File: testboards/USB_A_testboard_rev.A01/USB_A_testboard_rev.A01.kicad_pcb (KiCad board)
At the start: 2 copper layers, 18 x 12 mm, 10 parts, among them J1 USB_A_PCB_Edge_receptacle, J2 Conn_01x04, U1 USBLC6-2SC6

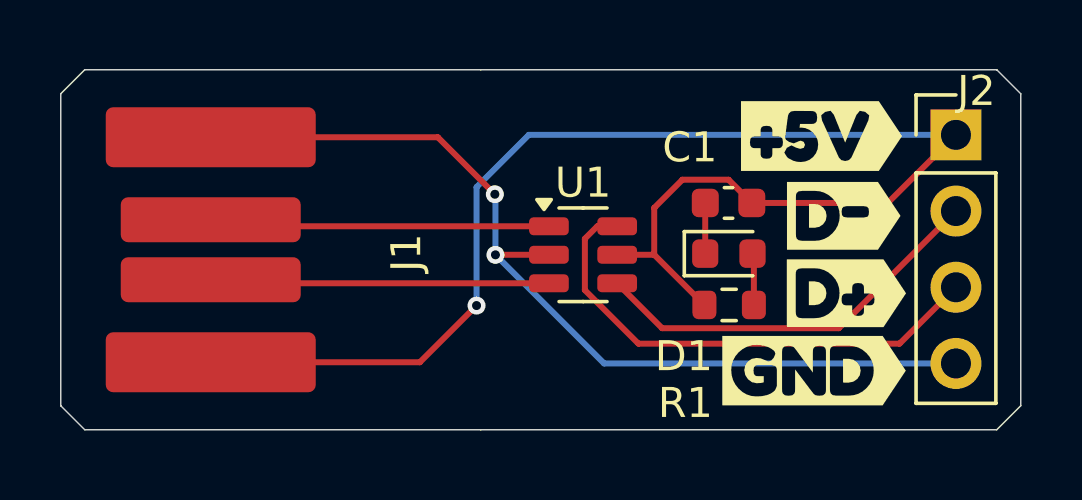
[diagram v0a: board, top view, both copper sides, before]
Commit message: Re-work test board to minimal USB-A PCB Plug
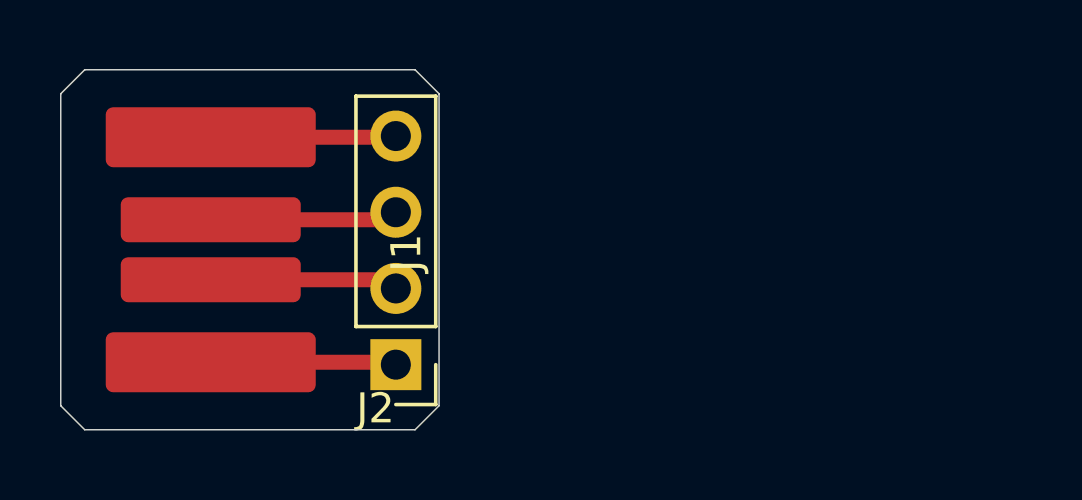
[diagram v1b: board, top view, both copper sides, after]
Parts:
- removed C1: 0.1u, Capacitor_SMD:C_0603_1608Metric
- removed D1: GREEN, LED_SMD:LED_0603_1608Metric
- removed R1: 1K, Resistor_SMD:R_0603_1608Metric
- removed U1: USBLC6-2SC6, Package_TO_SOT_SMD:SOT-23-6
- kibuzzard-65ECED05, kibuzzard-65ECED21, kibuzzard-65ECED2E, kibuzzard-65ECED44: moved to B.Cu
- moved J2 20.2 mm to (131.6, 80.7), turned to 180 degrees
- moved kibuzzard-65ECED44 20.0 mm to (127.1, 73.0)
- moved kibuzzard-65ECED05 20.0 mm to (127.3, 80.9)
- moved kibuzzard-65ECED2E 18.6 mm to (128.2, 75.6)
- moved kibuzzard-65ECED21 18.6 mm to (128.1, 78.2)
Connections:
- J1 pad 2: Net-(J1-D-) -> /mD_N
- J1 pad 3: Net-(J1-D+) -> /mD_P
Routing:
- net +5V_USB: track 47.2 -> 6.20 mm, vias 1 -> 0
- net GNDD: track 32.6 -> 6.19 mm, vias 2 -> 0
- net Net-(J1-D+): track 11.4 -> 0.00 mm
- net Net-(J1-D-): track 11.3 -> 0.00 mm
- net /mD_P: track 16.8 -> 6.27 mm
- net /mD_N: track 13.5 -> 6.29 mm
- net Net-(D1-A): track 1.73 -> 0.00 mm
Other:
- board size 18 x 12 mm -> 11.8 x 12 mm
